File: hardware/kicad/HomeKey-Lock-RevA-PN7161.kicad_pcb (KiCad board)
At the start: 4 copper layers, 150 x 75 mm, 120 parts, among them J1 BATTERY 3S 9.0-12.6V, J2 USB-C USB2, J3 EXT ANT DNP, J4 DS3115 SERVO, Q1 AO4407A, SW1 RESET, SW2 BOOT, SW3 SERVICE, U1 AP63205WU-7 5V, U2 USBLC6-2SC6, U3 AP63203WU-7 3V3, U4 ESP32-C6-MINI-1-N4, U5 PN7161B1HN/C100E, U6 TPS565201DDCR, X1 27.12MHz 10pF

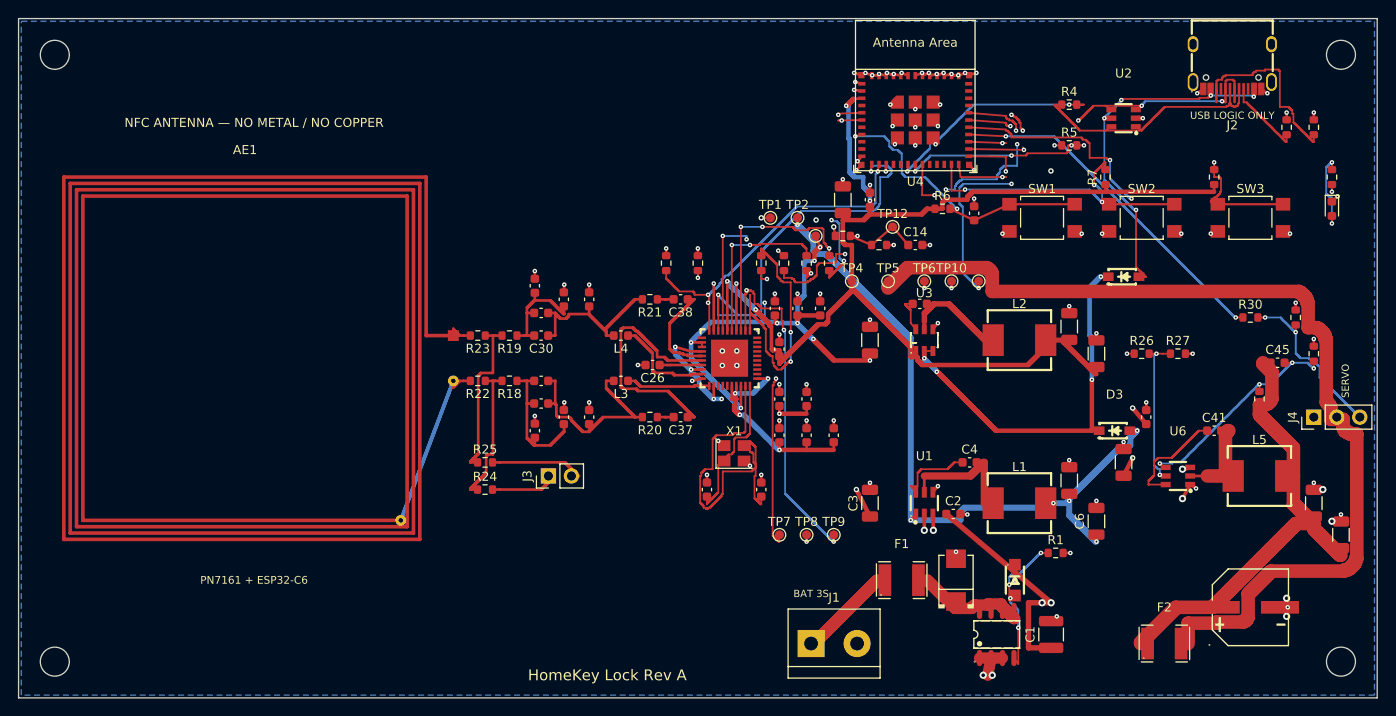
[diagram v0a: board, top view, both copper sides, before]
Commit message: Fix the router's pad obstacles and stop nets sealing each other's escapes
Two router defects, found while retesting the U6 placement from #3.

**Pad obstacles were the wrong shape on 92 of 364 pads.**  all_pad_points
computed each pad's rotation as footprint angle plus pad angle, but
generate_board.py bakes the footprint rotation into the children of everything
in NATIVE_CHILD_ANGLE_REFS -- every synced passive -- so for those it was
counted twice.  A quarter turn transposes the rectangle: C10's 1.8 x 1.15 mm
pad was blocked as 1.15 x 1.8, C1's by 1.55 mm.  The router was therefore
solving against a wrong map board-wide, and free to lay a 0.5 mm SYS_5V trace
with its centreline 0.100 mm from a foreign pad -- 0.150 mm of copper-to-copper
overlap.  audit_board.pad_geometry has always had the right rule; this is the
same one, and it takes the count of under-blocked pads to zero.

Nothing has ever shipped wrong: audit_board.py runs first in build_release and
fails on any short.  But it means the geometry audit has been catching a class
of error the router should not have been producing, and it explains why moving
a part could turn a clean board into one with three copper shorts.

**Nets could seal each other's escapes.**  Fanout runs for every net before any
is routed, so all endpoints are known; reserve a 0.5 mm disc around each, owned
by its own net.  Without it the router is coupled across the whole board:
moving R29 next to U6 rerouted SERVO_6V_OUT -- 116 mm, half the board -- so
that it passed 0.311 mm from U3's 3V3 escape 28 mm away, and 3V3 then reached
none of its eleven remaining endpoints (#3).  With it, that same move routes.

Both are steps 1 and 2 of the plan in #3.  Step 3, retesting the U6 placement,
is what turned up the pad bug: R29 routed but produced three F.Cu shorts, all
of them a wide trace grazing a transposed pad rectangle.

Board changes -- the obstacle map is different, so the routing is -- and passes
the whole gate: KiCad 10.0.6 DRC 0 violatio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
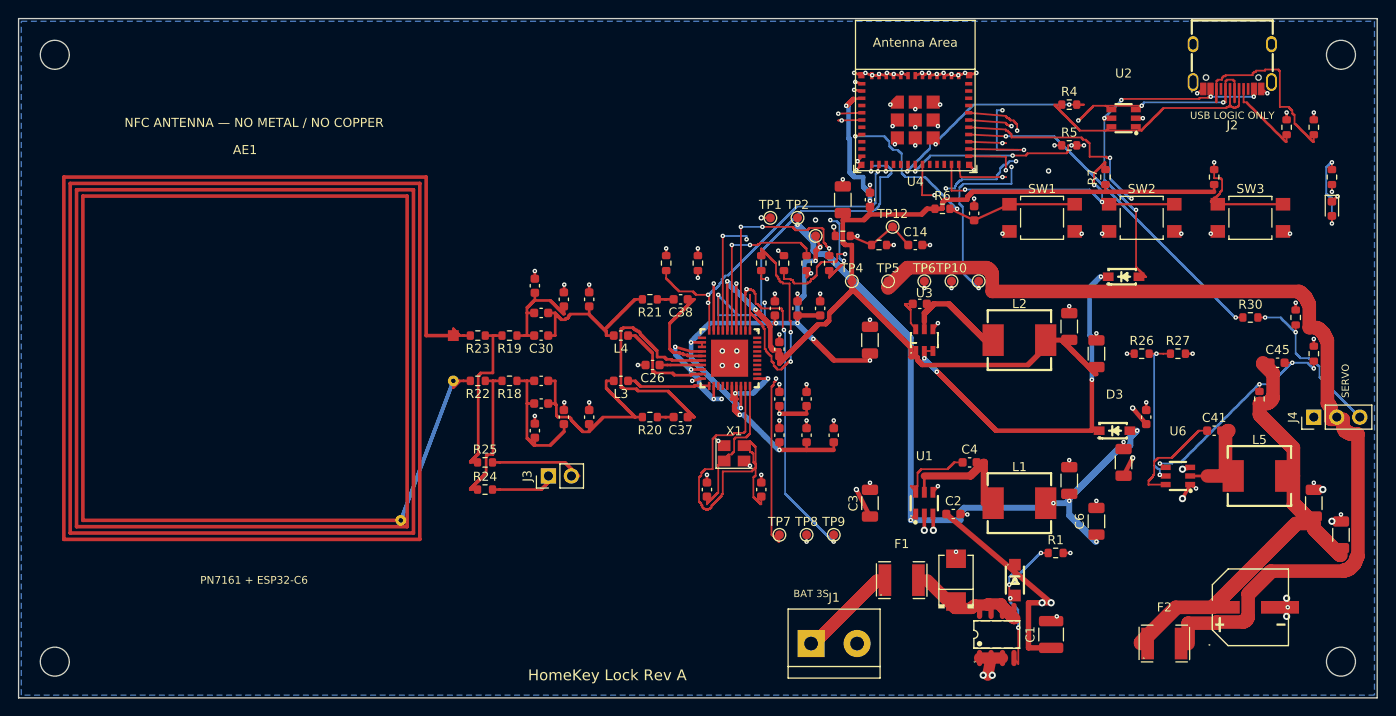
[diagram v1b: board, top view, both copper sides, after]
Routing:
- net PN_MOSI: track 54.8 -> 57.0 mm, vias 5 -> 4
- net XTAL2: track 43.0 -> 43.8 mm
- net SYS_5V: track 116.5 -> 115.9 mm

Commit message: Move the U6 feedback divider to VFB (13.31/20.12 -> 4.39/3.43 mm)
Step 3 of #3, and the first placement the router has accepted since the pour.
R28 and R29 set the servo rail through TPS565201's VFB pin; they were 13 and
20 mm from it.

This only became possible with the two router fixes in e5a5377.  Before them
the same move collapsed 3V3 to zero routed edges 28 mm away, and once that was
fixed it produced three copper shorts, all of them a wide trace grazing a
transposed pad rectangle.

U6's reference designator moves to F.Fab: it sits 4.95 mm above the part, which
is where the divider now lives, and R29's pad clips it.  The divider has to be
at VFB, so the silk is what moves.  57 designators on this board are already
fab-only for the same reason, U5 among them.

Against #3's acceptance gate:

  R28 -> U6.4 VFB     4.39 mm    (<= 8, target <= 3)   met
  R29 -> U6.4 VFB     3.43 mm    (<= 8, target <= 3)   met
  SW_SERVO extent     4.75 x 5.00 mm  (<= 4.8 x 5.0)   met
  BST_SERVO extent    6.47 x 6.00 mm  (<= 6.5 x 6.0)   met
  C45 with the divider                                 not met
  SERVO_FB extent    17.40 x 14.30 mm (<= 8 x 8)       not met

The two open rows are one item: C45, the DNP feedforward across R28, is still
where it was, and it alone stretches SERVO_FB back across the board.  Placing
it is not a placement problem -- the search finds a legal spot 4.43 mm from
VFB -- but every candidate so far fails the gate:

  * placed jointly with R28/R29, all three move and SW_SERVO stops routing;
  * placed against the accepted divider, a SERVO_FB via grazes a GND track by
    0.008 mm^2 and audit_board rejects the board.

That second one has the same shape as the pad bug just fixed: a clearance
check sized for the narrowest trace, this time in the via placement path.
Worth fixing there rather than working around here, so C45 stays put and the
gate row stays open.  Recorded in #3.

KiCad 10.0.6: 0 DRC violations, 0 unconnected, no rule suppressed; geometry
au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
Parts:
- moved R29 18.1 mm to (126.9, 45.3)
- moved R28 17.9 mm to (122.4, 52.3), turned to 0 degrees
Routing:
- net SERVO_6V: track 70.9 -> 91.8 mm
- net PN_MOSI: track 57.0 -> 42.5 mm, vias 4 -> 3
- net SERVO_6V_OUT: track 116.7 -> 125.3 mm
- net UART_RX: track 32.6 -> 28.9 mm
- net UART_TX: track 37.6 -> 35.1 mm, vias 4 -> 2
- net SERVO_FB: track 32.0 -> 34.0 mm
- net SYS_5V: track 115.9 -> 117.7 mm, vias 12 -> 10
- net SERVO_EN: track 44.0 -> 43.0 mm, vias 3 -> 2
- net BOOT: track 37.1 -> 36.1 mm
- net 3V3: track 159.1 -> 160.0 mm, vias 4 -> 7
- net SERVO_EN_IC: track 17.6 -> 18.4 mm
- net PN_SCK: track 44.5 -> 44.0 mm
- net GND: track 93.6 -> 93.7 mm, vias 105 -> 104

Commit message: Bring C45 to the feedback node; #3's acceptance gate is met
The remaining two rows of #3 were one item: C45, the DNP feedforward across
R28, still 17.48 mm from VFB and stretching SERVO_FB back across the board.

It failed twice before, and the second failure was mine, not the router's.  A
SERVO_FB via appeared to graze a GND track, so I widened the router's via-fit
margin -- on the reasoning that its 0.03 mm term is a quarter of GRID and can
be rounded away.  The baseline survived that, but the real offender turned out
to be C45's *own pad*, 0.025 mm from a 0.8 mm ground via that was already
there.  No amount of rerouting fixes a pad.  The margin change is reverted: the
reasoning about GRID may well be right, but it was not what was happening here
and an unproven tightening of the router is not worth carrying.

The actual bug was in local_passive_placer.py: its lane reservations read only
track segments and skipped GND outright, so vias were invisible to it.  A via
is a hole and a pad, not a lane -- nothing may sit on one, whatever its net.

Two designators move, each by the mechanism the project already has for it:

  * U6 to F.Fab via FAB_ONLY_REFERENCES.  Its designator sits 4.95 mm above
    the part, where the divider now is.
  * C45 to the _FabRef library variant via PASSIVE_FAB_REF_REFS.  Rotating a
    0603 by 90 degrees turns its designator onto its own pads.  Putting it in
    FAB_ONLY_REFERENCES instead worked but edits the footprint in place, and
    KiCad then reports lib_footprint_mismatch; the manifest's variant
    mechanism selects a library footprint that already matches.

#3's acceptance gate, all six rows:

  R28 -> U6.4 VFB     13.31 -> 4.39 mm     (<= 8, target <= 3)   met
  R29 -> U6.4 VFB     20.12 -> 3.43 mm     (<= 8, target <= 3)   met
  C45 -> U6.4 VFB     17.48 -> 5.11 mm     (with the divider)    met
  SERVO_FB extent     17.40 x 14.30 -> 6.92 x 7.15 mm  (<= 8x8)  met
  SW_SERVO extent     4.75 x 5.00 mm       (<= 4.8 x 5.0)        met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
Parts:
- C45: footprint HomeKey_RevA:C_0603_1608Metric -> HomeKey_RevA:C_0603_1608Metric_FabRef
- moved C45 18.3 mm to (130.2, 54.0), turned to 90 degrees
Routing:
- net SERVO_6V: track 91.8 -> 71.3 mm
- net SERVO_FB: track 34.0 -> 18.8 mm
